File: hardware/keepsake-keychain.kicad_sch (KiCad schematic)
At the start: 95 parts, among them Q1 MMFTP4042K, Q2 MMFTP4042K, Q3 MMFTP4042K, Q4 MMFTP4042K, SW1 SPDT Power Switch, SW2 PTS636 SK25J SMTR LFS, U1 74HC595, U2 74HC595, U3 74HC595, U4 Op Amp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

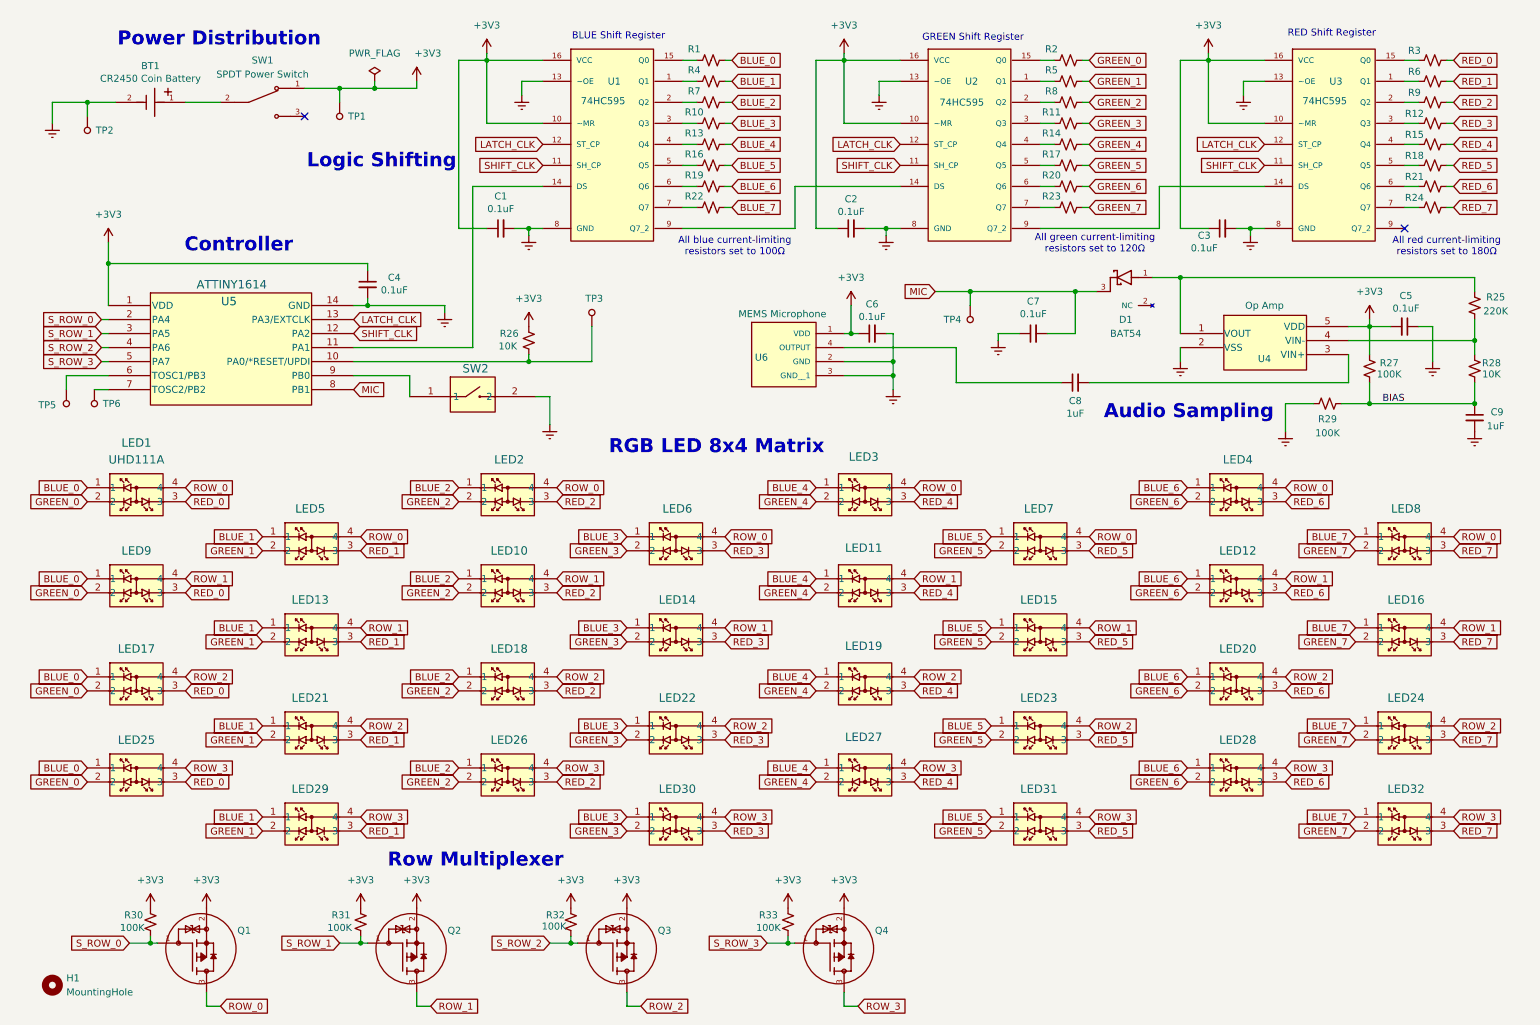
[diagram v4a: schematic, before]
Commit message: Fix errors from unassigned pins
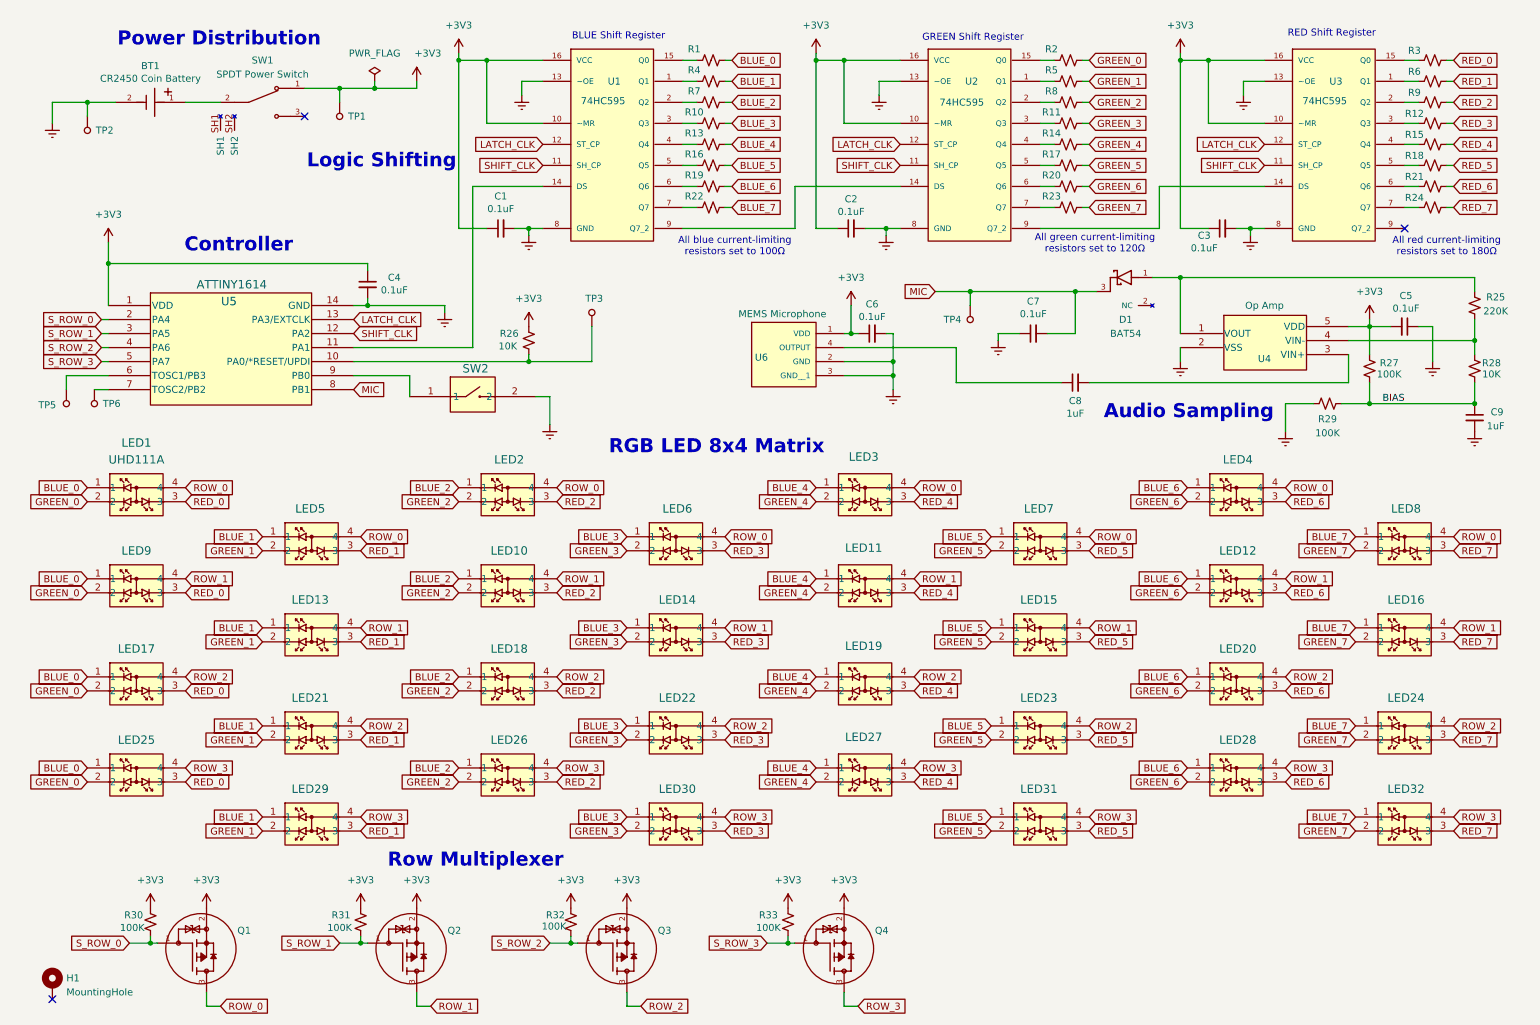
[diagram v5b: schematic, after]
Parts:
- H1: footprint MountingHole:MountingHole_3.2mm_M3_Pad_Via -> MountingHole:MountingHole_3.5mm_Pad_TopBottom; symbol Mechanical:MountingHole -> Mechanical:MountingHole_Pad
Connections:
- no-connect marks 2 -> 3
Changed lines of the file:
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@@
 	)
 	(junction
+		(at 157.48 22.86)
+		(diameter 0)
+		(color 0 0 0 0)
+	)
+	(junction
 		(at 152.4 182.88)
 		(diameter 0)
@@
 		(color 0 0 0 0)
 	)
+	(junction
+		(at 92.71 22.86)
+		(diameter 0)
+		(color 0 0 0 0)
+	)
+	(junction
+		(at 223.52 22.86)
+		(diameter 0)
+		(color 0 0 0 0)
+	)
+	(no_connect
+		(at 19.05 193.04)
+	)
 	(no_connect
 		(at 64.77 33.02)
@@
 	(wire
 		(pts
-			(xy 157.48 22.86) (xy 162.56 22.86)
-		)
-		(stroke
-			(width 0)
-			(type default)
-		)
-	)
-	(wire
-		(pts
 			(xy 162.56 80.01) (xy 171.45 80.01)
 		)
@@
 	(wire
 		(pts
-			(xy 228.6 21.59) (xy 228.6 22.86)
+			(xy 223.52 21.59) (xy 223.52 22.86)
 		)
 		(stroke
@@
 	(wire
 		(pts
-			(xy 97.79 22.86) (xy 97.79 21.59)
+			(xy 92.71 22.86) (xy 92.71 21.59)
 		)
 		(stroke
@@
 	(wire
 		(pts
+			(xy 157.48 22.86) (xy 162.56 22.86)
+		)
+		(stroke
+			(width 0)
+			(type default)
+		)
+	)
+	(wire
+		(pts
 			(xy 207.01 81.28) (xy 254 81.28)
 		)
@@
 	(wire
 		(pts
-			(xy 162.56 21.59) (xy 162.56 22.86)
+			(xy 157.48 21.59) (xy 157.48 22.86)
 		)
 		(stroke
@@
 	)
 	(symbol
-		(lib_id "Mechanical:MountingHole")
+		(lib_id "Mechanical:MountingHole_Pad")
 		(at 19.05 190.5 0)
 		(unit 1)
@@
 			)
 		)
-		(property "Footprint" "MountingHole:MountingHole_3.2mm_M3_Pad_Via"
+		(property "Footprint" "MountingHole:MountingHole_3.5mm_Pad_TopBottom"
 			(at 19.05 190.5 0)
 			(effects
@@
 			)
 		)
-		(property "Description" "Mounting Hole without connection"
+		(property "Description" "Mounting Hole with connection"
 			(at 19.05 190.5 0)
 			(effects
@@
 			)
 		)
+		(pin "1"
+		)
 		(instances
 			(project ""
@@
 		(pin "3"
 		)
+		(pin "SH2"
+		)
+		(pin "SH1"
+		)
 		(instances
 			(project ""
@@
 	(symbol
 		(lib_id "power:+3V3")
-		(at 97.79 21.59 0)
+		(at 92.71 21.59 0)
 		(unit 1)
 		(exclude_from_sim no)
@@
 		(fields_autoplaced yes)
 		(property "Reference" "#PWR01"
-			(at 97.79 25.4 0)
+			(at 92.71 25.4 0)
 			(effects
 				(font
@@
 		)
 		(property "Value" "+3V3"
-			(at 97.79 16.51 0)
+			(at 92.71 16.51 0)
 			(effects
 				(font
@@
 		)
 		(property "Footprint" ""
-			(at 97.79 21.59 0)
+			(at 92.71 21.59 0)
 			(effects
 				(font
@@
 		)
 		(property "Datasheet" ""
-			(at 97.79 21.59 0)
+			(at 92.71 21.59 0)
 			(effects
 				(font
@@
 		)
 		(property "Description" "Power symbol creates a global label with name \"+3V3\""
-			(at 97.79 21.59 0)
+			(at 92.71 21.59 0)
 			(effects
 				(font
@@
 	(symbol
 		(lib_id "power:+3V3")
-		(at 162.56 21.59 0)
+		(at 157.48 21.59 0)
 		(unit 1)
 		(exclude_from_sim no)
@@
 		(fields_autoplaced yes)
 		(property "Reference" "#PWR02"
-			(at 162.56 25.4 0)
+			(at 157.48 25.4 0)
 			(effects
 				(font
@@
 		)
 		(property "Value" "+3V3"
-			(at 162.56 16.51 0)
+			(at 157.48 16.51 0)
 			(effects
 				(font
@@
 		)
 		(property "Footprint" ""
-			(at 162.56 21.59 0)
+			(at 157.48 21.59 0)
 			(effects
 				(font
@@
 		)
 		(property "Datasheet" ""
-			(at 162.56 21.59 0)
+			(at 157.48 21.59 0)
 			(effects
 				(font
@@
 		)
 		(property "Description" "Power symbol creates a global label with name \"+3V3\""
-			(at 162.56 21.59 0)
+			(at 157.48 21.59 0)
 			(effects
 				(font
@@
 	(symbol
 		(lib_id "power:+3V3")
-		(at 228.6 21.59 0)
+		(at 223.52 21.59 0)
 		(unit 1)
 		(exclude_from_sim no)
@@
 		(fields_autoplaced yes)
 		(property "Reference" "#PWR03"
-			(at 228.6 25.4 0)
+			(at 223.52 25.4 0)
 			(effects
 				(font
@@
 		)
 		(property "Value" "+3V3"
-			(at 228.6 16.51 0)
+			(at 223.52 16.51 0)
 			(effects
 				(font
@@
 		)
 		(property "Footprint" ""
-			(at 228.6 21.59 0)
+			(at 223.52 21.59 0)
 			(effects
 				(font
@@
 		)
 		(property "Datasheet" ""
-			(at 228.6 21.59 0)
+			(at 223.52 21.59 0)
 			(effects
 				(font
@@
 		)
 		(property "Description" "Power symbol creates a global label with name \"+3V3\""
-			(at 228.6 21.59 0)
+			(at 223.52 21.59 0)
 			(effects
 				(font

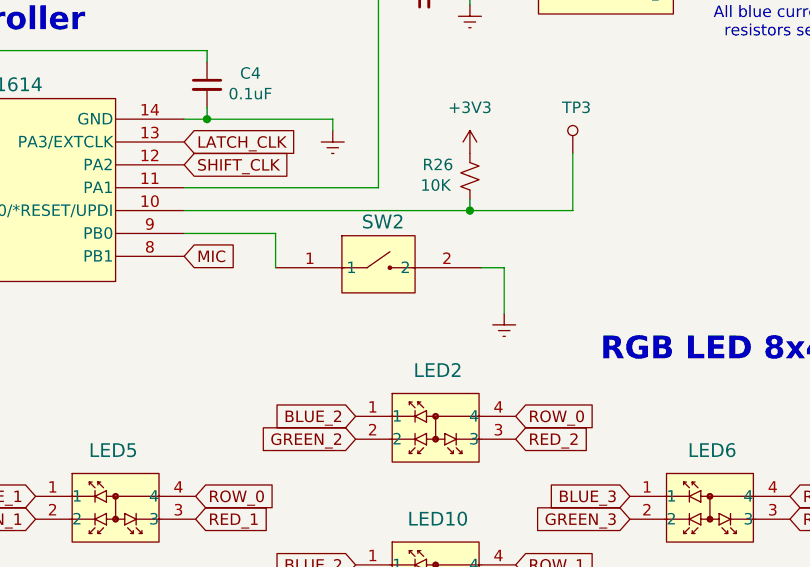
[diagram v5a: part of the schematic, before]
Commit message: Replace tactile push button for stable, lower profile
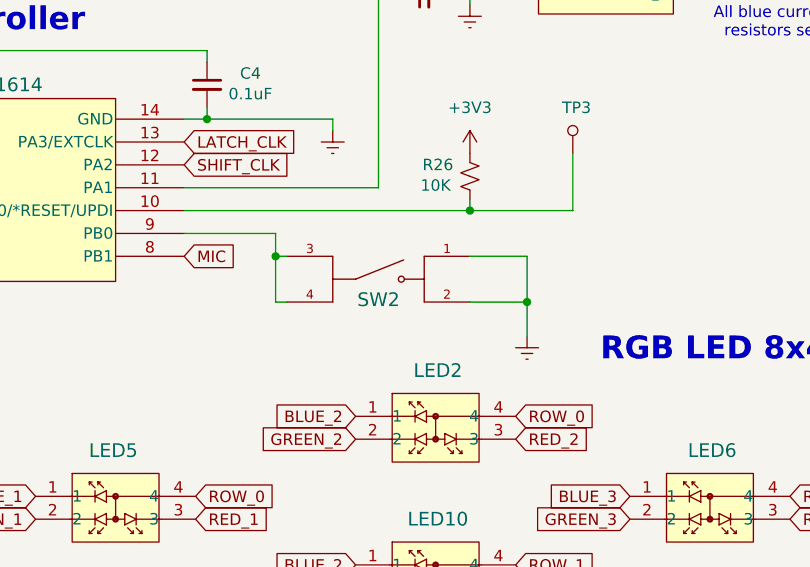
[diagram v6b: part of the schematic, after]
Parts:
- SW2: footprint 0_Tactile_Push_Button:SW_PTS636_SM43J_SMTR_LFS -> 0_Tactile_Push_Button:SW_TS18-5-15-SL-160-SMT-TR; symbol 0_Tactile_Push_Button:PTS636_SK25J_SMTR_LFS -> 0_Tactile_Push_Button:TS18-5-15-SL-160-SMT-TR; MANUFACTURER (none) -> Same Sky; PARTREV (none) -> 1.02; STANDARD (none) -> Manufacturer Recommendations
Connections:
- net GND: now also SW2.1
- net at U5.9 (PB0): now also SW2.3, SW2.4; no longer SW2.1
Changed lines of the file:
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@@
 	)
 	(junction
+		(at 83.82 82.55)
+		(diameter 0)
+		(color 0 0 0 0)
+	)
+	(junction
 		(at 97.79 22.86)
 		(diameter 0)
@@
 		(color 0 0 0 0)
 	)
+	(junction
+		(at 111.76 87.63)
+		(diameter 0)
+		(color 0 0 0 0)
+	)
 	(no_connect
 		(at 19.05 193.04)
@@
 	(wire
 		(pts
+			(xy 105.41 87.63) (xy 111.76 87.63)
+		)
+		(stroke
+			(width 0)
+			(type default)
+		)
+	)
+	(wire
+		(pts
 			(xy 223.52 53.34) (xy 223.52 22.86)
 		)
@@
 	(wire
 		(pts
+			(xy 111.76 87.63) (xy 111.76 91.44)
+		)
+		(stroke
+			(width 0)
+			(type default)
+		)
+	)
+	(wire
+		(pts
 			(xy 95.25 74.93) (xy 95.25 45.72)
 		)
@@
 	(wire
 		(pts
+			(xy 105.41 82.55) (xy 111.76 82.55)
+		)
+		(stroke
+			(width 0)
+			(type default)
+		)
+	)
+	(wire
+		(pts
 			(xy 153.67 53.34) (xy 153.67 45.72)
 		)
@@
 	(wire
 		(pts
+			(xy 83.82 80.01) (xy 83.82 82.55)
+		)
+		(stroke
+			(width 0)
+			(type default)
+		)
+	)
+	(wire
+		(pts
 			(xy 205.74 45.72) (xy 207.01 45.72)
 		)
@@
 	(wire
 		(pts
-			(xy 83.82 83.82) (xy 83.82 80.01)
+			(xy 264.16 26.67) (xy 266.7 26.67)
 		)
 		(stroke
@@
 	(wire
 		(pts
-			(xy 264.16 26.67) (xy 266.7 26.67)
+			(xy 135.89 49.53) (xy 133.35 49.53)
 		)
 		(stroke
@@
 	(wire
 		(pts
-			(xy 135.89 49.53) (xy 133.35 49.53)
+			(xy 135.89 41.91) (xy 133.35 41.91)
 		)
 		(stroke
@@
 	(wire
 		(pts
-			(xy 135.89 41.91) (xy 133.35 41.91)
+			(xy 171.45 80.01) (xy 171.45 82.55)
 		)
 		(stroke
@@
 	(wire
 		(pts
-			(xy 171.45 80.01) (xy 171.45 82.55)
+			(xy 204.47 64.77) (xy 204.47 72.39)
 		)
 		(stroke
@@
 	(wire
 		(pts
-			(xy 204.47 64.77) (xy 204.47 72.39)
+			(xy 83.82 82.55) (xy 83.82 87.63)
 		)
 		(stroke
@@
 	(wire
 		(pts
-			(xy 106.68 83.82) (xy 109.22 83.82)
+			(xy 71.12 182.88) (xy 74.93 182.88)
 		)
 		(stroke
@@
 	(wire
 		(pts
-			(xy 71.12 182.88) (xy 74.93 182.88)
+			(xy 236.22 53.34) (xy 236.22 54.61)
 		)
 		(stroke
@@
 	(wire
 		(pts
-			(xy 236.22 53.34) (xy 236.22 54.61)
+			(xy 204.47 64.77) (xy 208.28 64.77)
 		)
 		(stroke
@@
 	(wire
 		(pts
-			(xy 204.47 64.77) (xy 208.28 64.77)
+			(xy 257.81 71.12) (xy 261.62 71.12)
 		)
 		(stroke
@@
 	(wire
 		(pts
-			(xy 257.81 71.12) (xy 261.62 71.12)
+			(xy 95.25 45.72) (xy 107.95 45.72)
 		)
 		(stroke
@@
 	(wire
 		(pts
-			(xy 95.25 45.72) (xy 107.95 45.72)
+			(xy 111.76 82.55) (xy 111.76 87.63)
 		)
 		(stroke
@@
 	(wire
 		(pts
+			(xy 83.82 87.63) (xy 85.09 87.63)
+		)
+		(stroke
+			(width 0)
+			(type default)
+		)
+	)
+	(wire
+		(pts
 			(xy 140.97 30.48) (xy 142.24 30.48)
 		)
@@
 	(wire
 		(pts
+			(xy 83.82 82.55) (xy 85.09 82.55)
+		)
+		(stroke
+			(width 0)
+			(type default)
+		)
+	)
+	(wire
+		(pts
 			(xy 223.52 74.93) (xy 223.52 77.47)
 		)
@@
 	(wire
 		(pts
-			(xy 109.22 83.82) (xy 109.22 88.9)
-		)
-		(stroke
-			(width 0)
-			(type default)
-		)
-	)
-	(wire
-		(pts
 			(xy 27.94 77.47) (xy 29.21 77.47)
 		)
@@
 	(symbol
 		(lib_id "power:GNDREF")
-		(at 109.22 88.9 0)
+		(at 111.76 91.44 0)
 		(unit 1)
 		(exclude_from_sim no)
@@
 		(dnp no)
 		(fields_autoplaced yes)
-		(property "Reference" "#PWR021"
-			(at 109.22 95.25 0)
+		(property "Reference" "#PWR023"
+			(at 111.76 97.79 0)
 			(effects
 				(font
@@
 		)
 		(property "Value" "GND"
-			(at 111.76 90.1699 0)
+			(at 114.3 92.7099 0)
 			(effects
 				(font
@@
 		)
 		(property "Footprint" ""
-			(at 109.22 88.9 0)
+			(at 111.76 91.44 0)
 			(effects
 				(font
@@
 		)
 		(property "Datasheet" ""
-			(at 109.22 88.9 0)
+			(at 111.76 91.44 0)
 			(effects
 				(font
@@
 		)
 		(property "Description" "Power symbol creates a global label with name \"GNDREF\" , reference supply ground"
-			(at 109.22 88.9 0)
+			(at 111.76 91.44 0)
 			(effects
 				(font
@@
 			(project "keepsake-keychain"
 				(path "/32670795-e352-430d-9b7f-c7f10ebe6399"
-					(reference "#PWR021")
+					(reference "#PWR023")
 					(unit 1)
 				)
@@
 		(dnp no)
 		(fields_autoplaced yes)
-		(property "Reference" "#PWR022"
+		(property "Reference" "#PWR021"
 			(at 242.57 96.52 0)
 			(effects
@@
 			(project "keepsake-keychain"
 				(path "/32670795-e352-430d-9b7f-c7f10ebe6399"
-					(reference "#PWR022")
+					(reference "#PWR021")
 					(unit 1)
 				)
@@
 		(dnp no)
 		(fields_autoplaced yes)
-		(property "Reference" "#PWR023"
+		(property "Reference" "#PWR022"
 			(at 276.86 96.52 0)
 			(effects
@@
 			(project "keepsake-keychain"
 				(path "/32670795-e352-430d-9b7f-c7f10ebe6399"
-					(reference "#PWR023")
+					(reference "#PWR022")
 					(unit 1)
 				)
@@
 	)
 	(symbol
-		(lib_id "0_Tactile_Push_Button:PTS636_SK25J_SMTR_LFS")
-		(at 76.2 83.82 0)
+		(lib_id "0_Tactile_Push_Button:TS18-5-15-SL-160-SMT-TR")
+		(at 95.25 85.09 0)
 		(unit 1)
 		(exclude_from_sim no)
@@
 		(dnp no)
 		(property "Reference" "SW2"
-			(at 95.758 78.74 0)
+			(at 95.25 87.376 0)
 			(effects
 				(font
@@
 		)
 		(property "Value" "PTS636 SK25J SMTR LFS"
-			(at 96.52 76.2 0)
+			(at 115.57 77.47 0)
 			(effects
 				(font
@@
 			)
 		)
-		(property "Footprint" "0_Tactile_Push_Button:SW_PTS636_SM43J_SMTR_LFS"
-			(at 76.2 83.82 0)
+		(property "Footprint" "0_Tactile_Push_Button:SW_TS18-5-15-SL-160-SMT-TR"
+			(at 95.25 85.09 0)
 			(effects
 				(font
 					(size 1.27 1.27)
-					(italic yes)
 				)
+				(justify bottom)
 				(hide yes)
 			)
 		)
-		(property "Datasheet" "PTS636 SK25J SMTR LFS"
-			(at 76.2 83.82 0)
+		(property "Datasheet" ""
+			(at 95.25 85.09 0)
 			(effects
 				(font
 					(size 1.27 1.27)
-					(italic yes)
 				)
 				(hide yes)
@@
 		)
 		(property "Description" ""
-			(at 76.2 83.82 0)
+			(at 95.25 85.09 0)
+			(effects
+				(font
+					(size 1.27 1.27)
+				)
+				(hide yes)
+			)
+		)
+		(property "STANDARD" "Manufacturer Recommendations"
+			(at 95.25 85.09 0)
+			(effects
+				(font
+					(size 1.27 1.27)
+				)
+				(justify bottom)
+				(hide yes)
+			)
+		)
+		(property "PARTREV" "1.02"
+			(at 95.25 85.09 0)
+			(effects
+				(font
+					(size 1.27 1.27)
+				)
+				(justify bottom)
+				(hide yes)
+			)
+		)
+		(property "MANUFACTURER" "Same Sky"
+			(at 95.25 85.09 0)
 			(effects
 				(font
 					(size 1.27 1.27)
 				)
+				(justify bottom)
 				(hide yes)
 			)
@@
 		(pin "1"
 		)
+		(pin "3"
+		)
+		(pin "4"
+		)
 		(instances

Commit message: Route all traces for controller
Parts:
- TP1, TP3: footprint TestPoint:TestPoint_THTPad_D1.5mm_Drill0.7mm -> TestPoint:TestPoint_THTPad_D2.0mm_Drill1.0mm
- TP2: footprint TestPoint:TestPoint_THTPad_D1.5mm_Drill0.7mm -> TestPoint:TestPoint_THTPad_2.0x2.0mm_Drill1.0mm
- TP4, TP5, TP6: footprint TestPoint:TestPoint_THTPad_D1.5mm_Drill0.7mm -> TestPoint:TestPoint_Pad_D1.0mm
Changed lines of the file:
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@@
 			)
 		)
-		(property "Footprint" "TestPoint:TestPoint_THTPad_D1.5mm_Drill0.7mm"
+		(property "Footprint" "TestPoint:TestPoint_THTPad_2.0x2.0mm_Drill1.0mm"
 			(at 30.48 30.48 0)
 			(effects
@@
 			)
 		)
-		(property "Footprint" "TestPoint:TestPoint_THTPad_D1.5mm_Drill0.7mm"
+		(property "Footprint" "TestPoint:TestPoint_THTPad_D2.0mm_Drill1.0mm"
 			(at 76.2 27.94 0)
 			(effects
@@
 			)
 		)
-		(property "Footprint" "TestPoint:TestPoint_THTPad_D1.5mm_Drill0.7mm"
+		(property "Footprint" "TestPoint:TestPoint_Pad_D1.0mm"
 			(at 31.75 80.01 0)
 			(effects
@@
 			)
 		)
-		(property "Footprint" "TestPoint:TestPoint_THTPad_D1.5mm_Drill0.7mm"
+		(property "Footprint" "TestPoint:TestPoint_Pad_D1.0mm"
 			(at 190.5 64.77 0)
 			(effects
@@
 			)
 		)
-		(property "Footprint" "TestPoint:TestPoint_THTPad_D1.5mm_Drill0.7mm"
+		(property "Footprint" "TestPoint:TestPoint_Pad_D1.0mm"
 			(at 26.67 80.01 0)
 			(effects
@@
 			)
 		)
-		(property "Footprint" "TestPoint:TestPoint_THTPad_D1.5mm_Drill0.7mm"
+		(property "Footprint" "TestPoint:TestPoint_THTPad_D2.0mm_Drill1.0mm"
 			(at 111.76 73.66 0)
 			(effects
